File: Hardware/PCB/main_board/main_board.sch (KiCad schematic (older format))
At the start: 0 parts

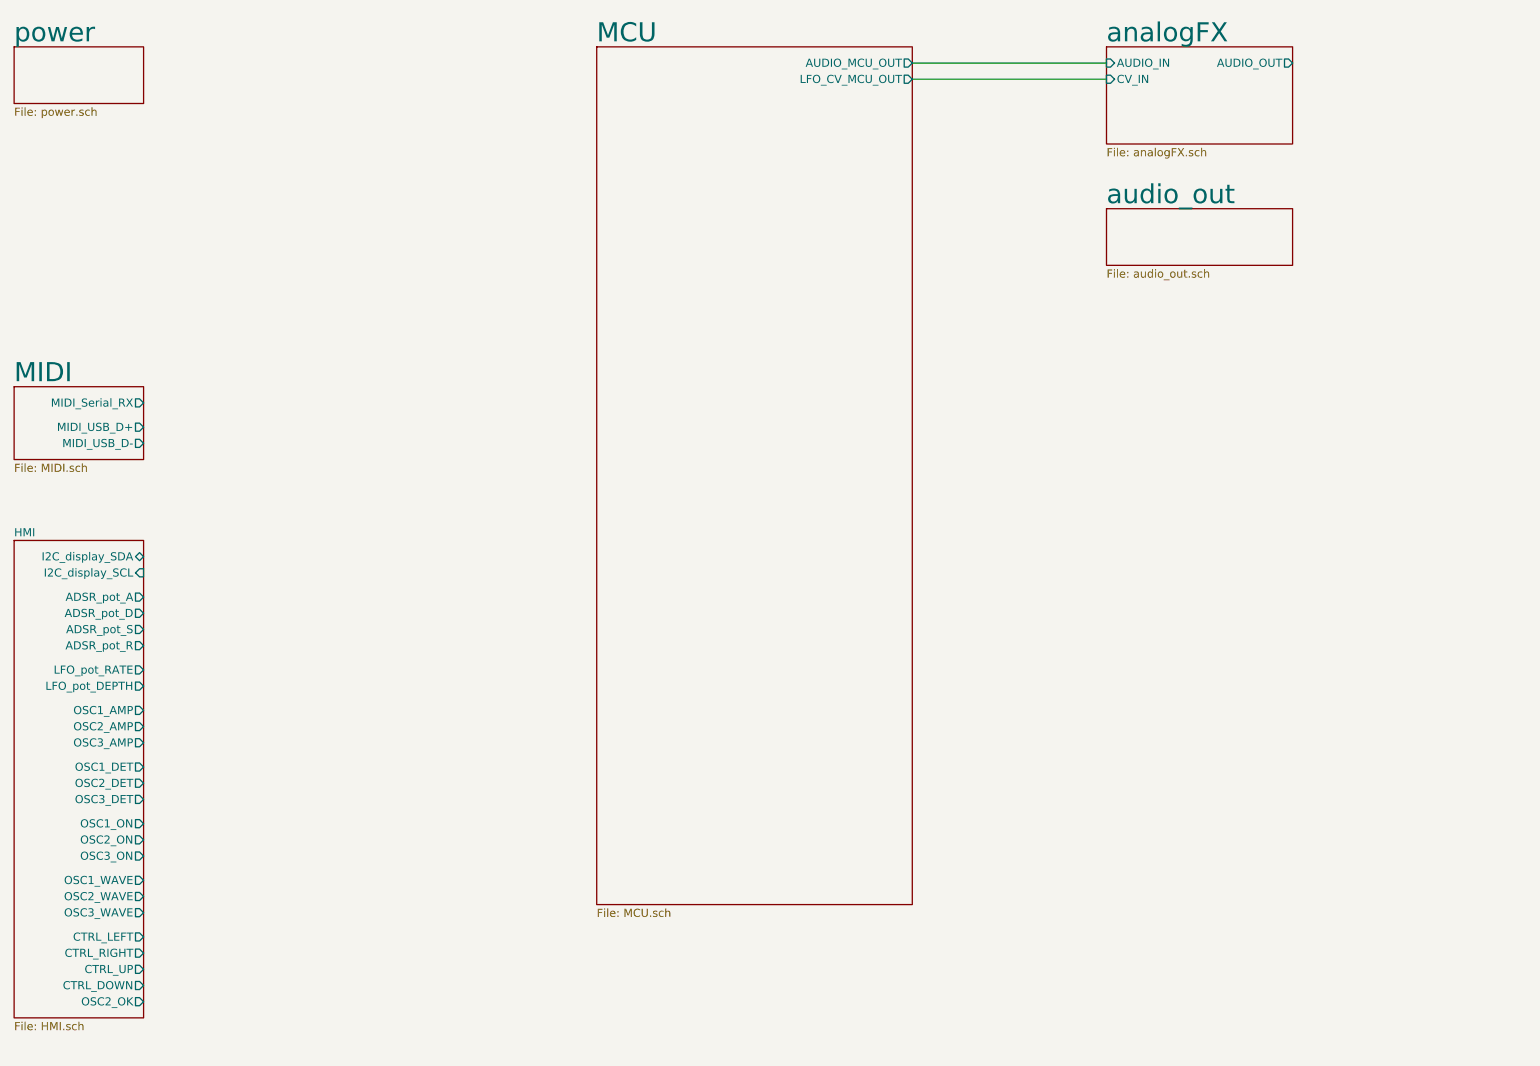
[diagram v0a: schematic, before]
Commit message: Place VCF components, I2C bus
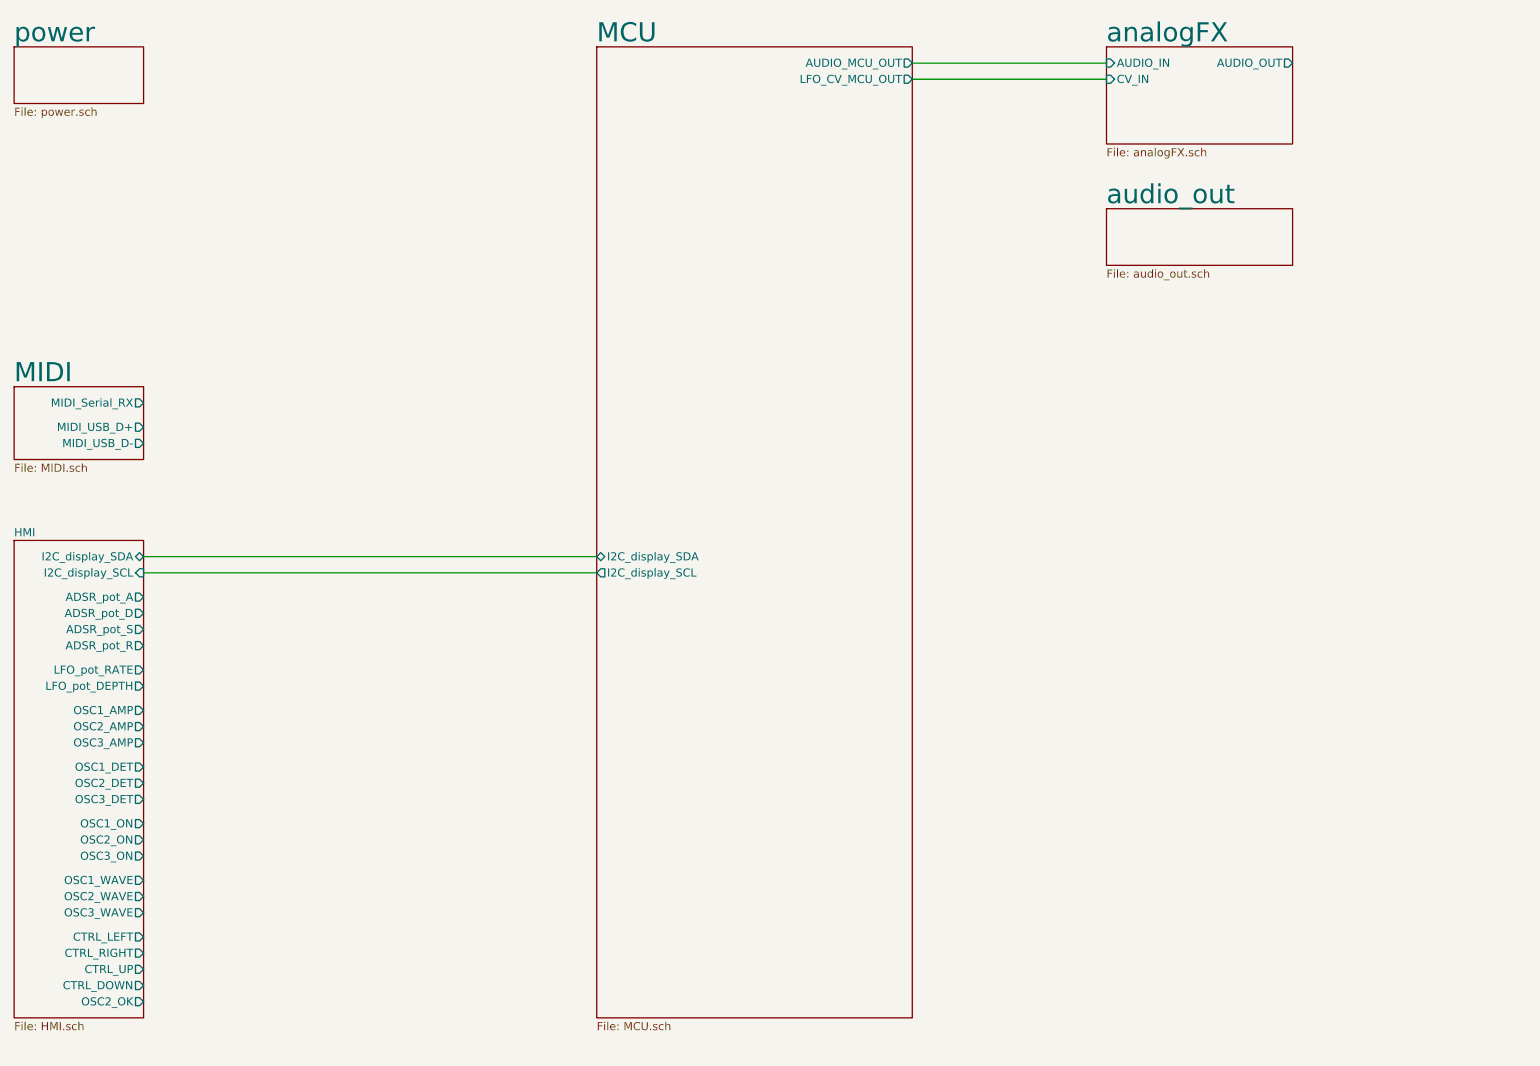
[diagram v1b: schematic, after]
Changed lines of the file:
@@
-$EndSheet
-$Sheet
-S 4800 1150 1950 5300
-U 5E658709
-F0 "MCU" 118
-F1 "MCU.sch" 50
-F2 "AUDIO_MCU_OUT" O R 6750 1250 50
-F3 "LFO_CV_MCU_OUT" O R 6750 1350 50
 $EndSheet
 $Sheet
@@
 F26 "LFO_pot_DEPTH" O R 2000 5100 50
 $EndSheet
+$Sheet
+S 4800 1150 1950 6000
+U 5E658709
+F0 "MCU" 118
+F1 "MCU.sch" 50
+F2 "AUDIO_MCU_OUT" O R 6750 1250 50
+F3 "LFO_CV_MCU_OUT" O R 6750 1350 50
+F4 "I2C_display_SCL" O L 4800 4400 50
+F5 "I2C_display_SDA" B L 4800 4300 50
+$EndSheet
+Wire Wire Line
+	2000 4300 4800 4300
+Wire Wire Line
+	4800 4400 2000 4400
 $EndSCHEMATC

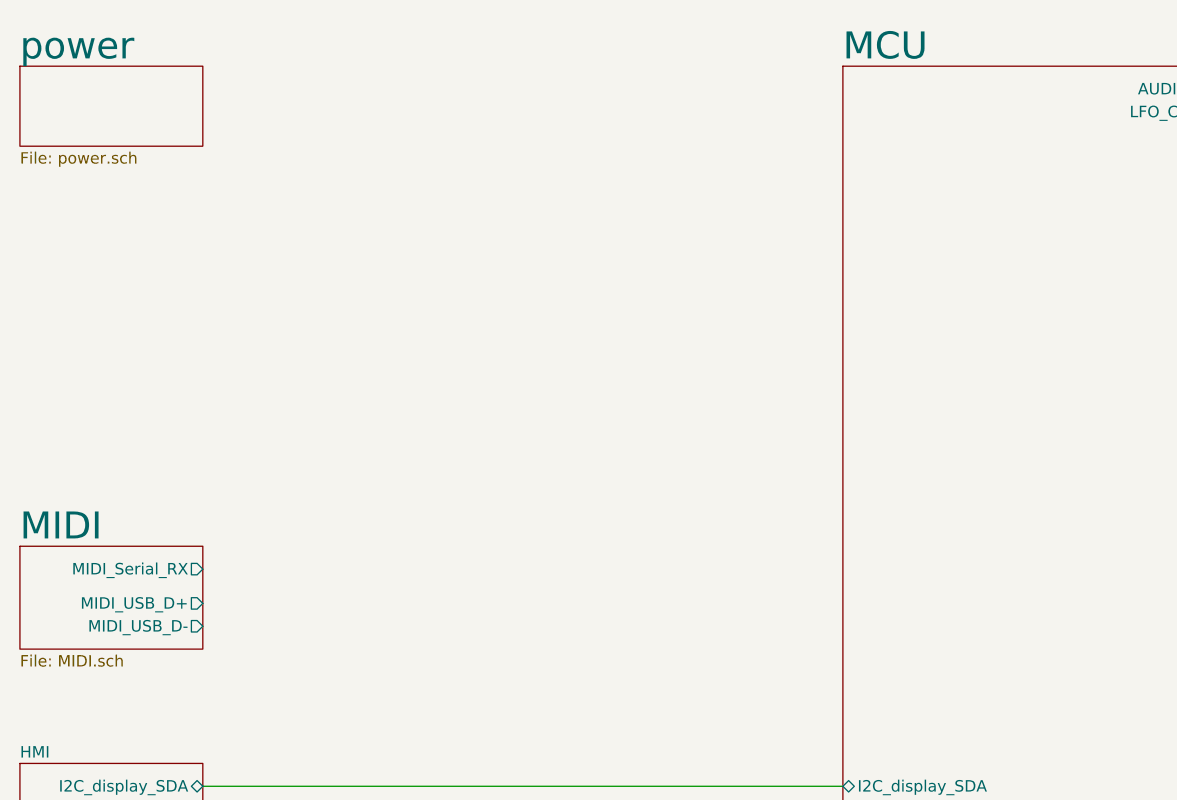
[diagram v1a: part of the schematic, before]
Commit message: Update 3D view
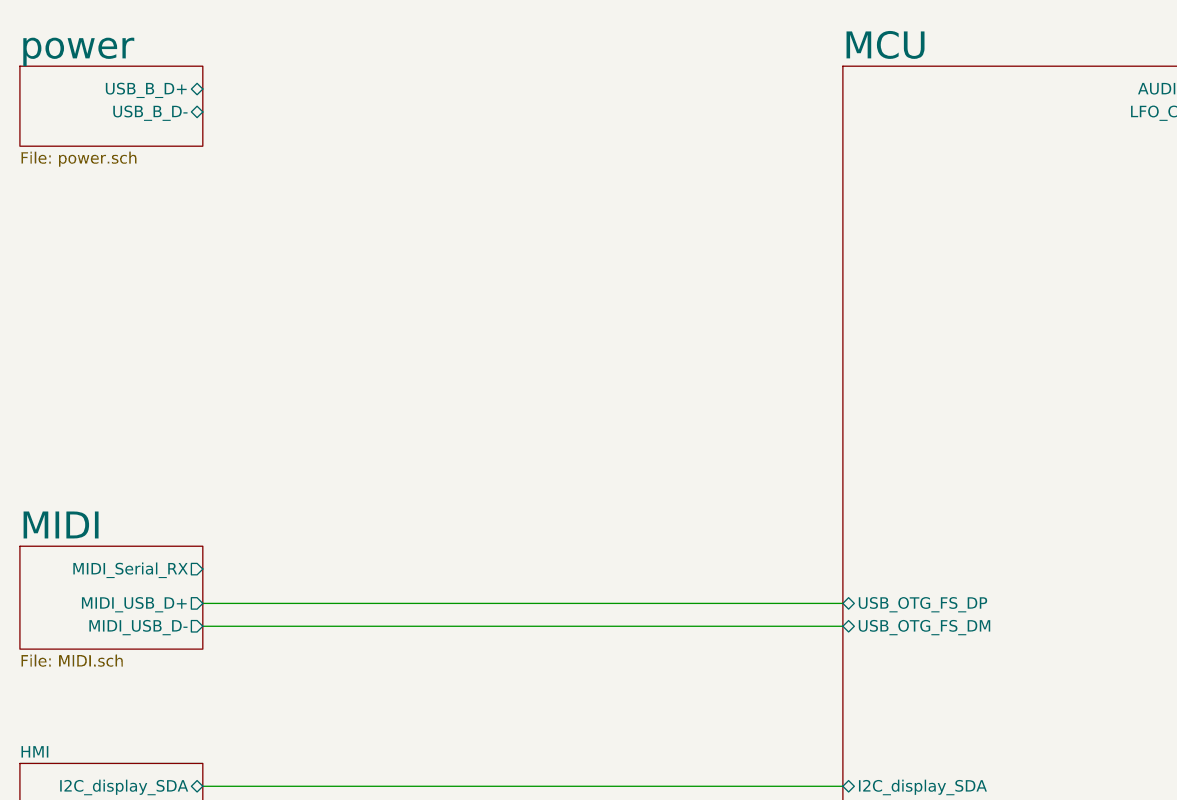
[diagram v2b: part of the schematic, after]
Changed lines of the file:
@@
 F0 "power" 118
 F1 "power.sch" 50
+F2 "USB_B_D+" B R 2000 1250 50
+F3 "USB_B_D-" B R 2000 1350 50
 $EndSheet
 $Sheet
@@
 F4 "I2C_display_SCL" O L 4800 4400 50
 F5 "I2C_display_SDA" B L 4800 4300 50
+F6 "USB_OTG_FS_DP" B L 4800 3500 50
+F7 "USB_OTG_FS_DM" B L 4800 3600 50
 $EndSheet
 Wire Wire Line
@@
 Wire Wire Line
 	4800 4400 2000 4400
+Wire Wire Line
+	2000 3500 4800 3500
+Wire Wire Line
+	2000 3600 4800 3600
 $EndSCHEMATC

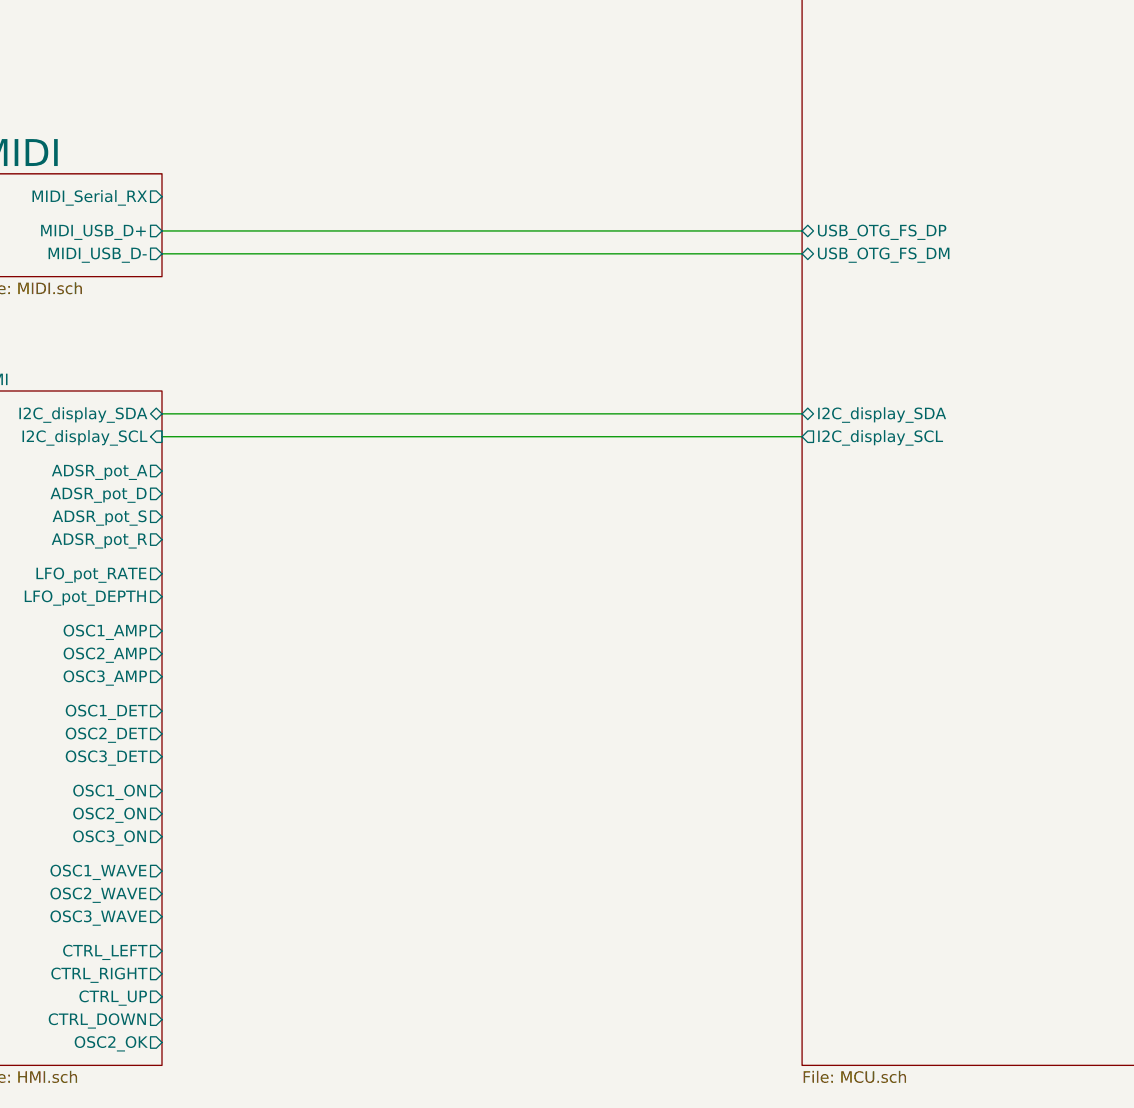
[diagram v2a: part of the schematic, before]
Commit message: Route GPIO
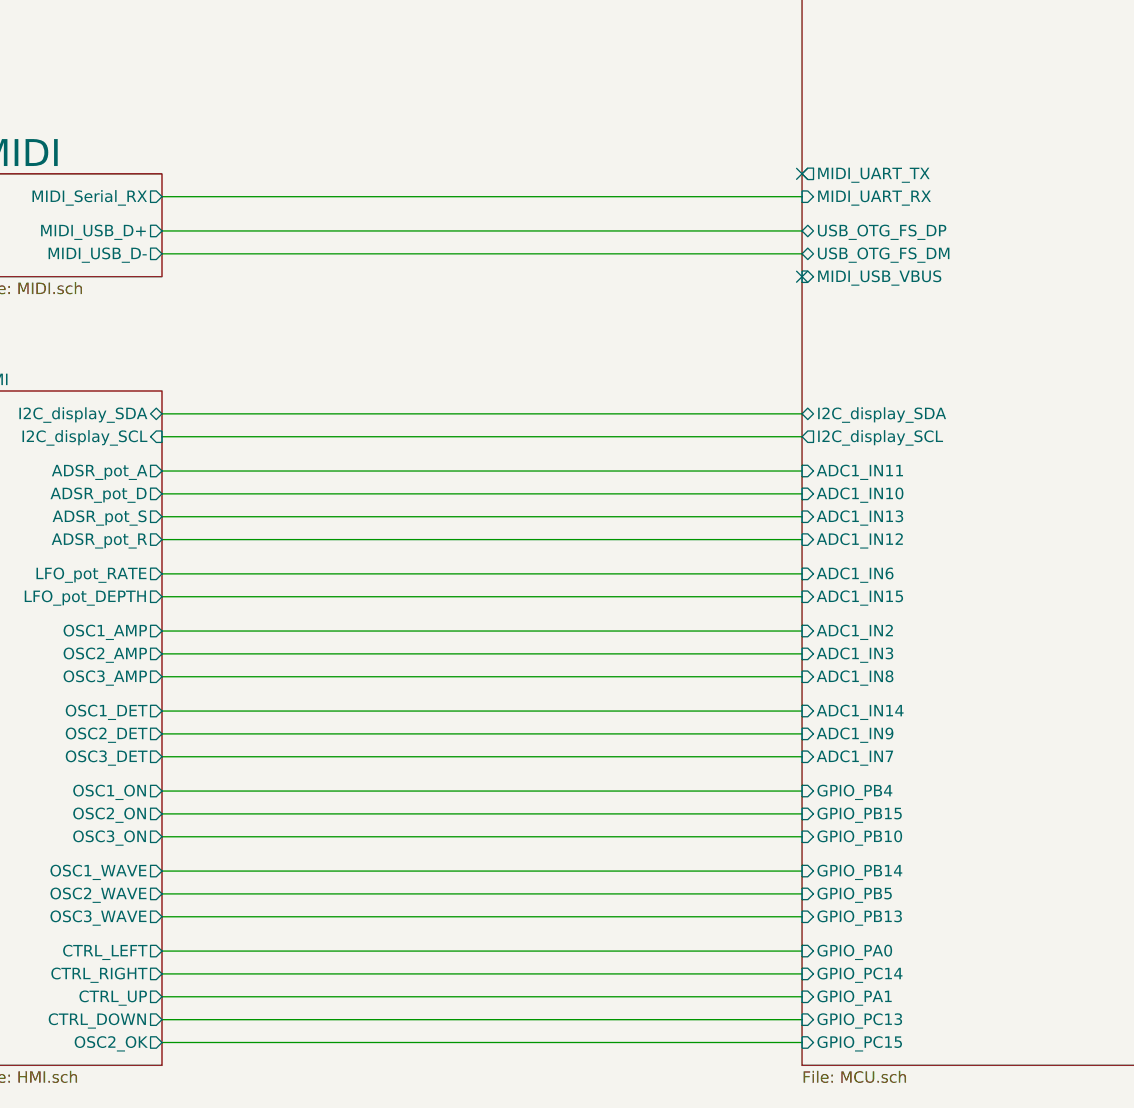
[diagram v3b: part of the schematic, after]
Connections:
- no-connect marks 0 -> 2
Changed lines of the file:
@@
 F26 "LFO_pot_DEPTH" O R 2000 5100 50
 $EndSheet
+Wire Wire Line
+	2000 4300 4800 4300
+Wire Wire Line
+	4800 4400 2000 4400
+Wire Wire Line
+	2000 3500 4800 3500
+Wire Wire Line
+	2000 3600 4800 3600
+Wire Wire Line
+	2000 5000 4800 5000
+Wire Wire Line
+	4800 5100 2000 5100
+Wire Wire Line
+	2000 4550 4800 4550
+Wire Wire Line
+	4800 4650 2000 4650
+Wire Wire Line
+	2000 4750 4800 4750
+Wire Wire Line
+	4800 4850 2000 4850
+Wire Wire Line
+	2000 5250 4800 5250
+Wire Wire Line
+	4800 5350 2000 5350
+Wire Wire Line
+	2000 5450 4800 5450
+Wire Wire Line
+	4800 5600 2000 5600
+Wire Wire Line
+	2000 5700 4800 5700
+Wire Wire Line
+	4800 5800 2000 5800
+Wire Wire Line
+	4800 6650 2000 6650
+Wire Wire Line
+	2000 6750 4800 6750
+Wire Wire Line
+	4800 6850 2000 6850
+Wire Wire Line
+	2000 6950 4800 6950
+Wire Wire Line
+	4800 7050 2000 7050
 $Sheet
 S 4800 1150 1950 6000
@@
 F6 "USB_OTG_FS_DP" B L 4800 3500 50
 F7 "USB_OTG_FS_DM" B L 4800 3600 50
+F8 "MIDI_UART_TX" O L 4800 3250 50
+F9 "MIDI_UART_RX" I L 4800 3350 50
+F10 "MIDI_USB_VBUS" I L 4800 3700 50
+F11 "ADC1_IN10" I L 4800 4650 50
+F12 "ADC1_IN11" I L 4800 4550 50
+F13 "ADC1_IN12" I L 4800 4850 50
+F14 "ADC1_IN13" I L 4800 4750 50
+F15 "ADC1_IN2" I L 4800 5250 50
+F16 "ADC1_IN3" I L 4800 5350 50
+F17 "ADC1_IN6" I L 4800 5000 50
+F18 "ADC1_IN7" I L 4800 5800 50
+F19 "ADC1_IN14" I L 4800 5600 50
+F20 "ADC1_IN15" I L 4800 5100 50
+F21 "ADC1_IN9" I L 4800 5700 50
+F22 "ADC1_IN8" I L 4800 5450 50
+F23 "GPIO_PA0" I L 4800 6650 50
+F24 "GPIO_PA1" I L 4800 6850 50
+F25 "GPIO_PC13" I L 4800 6950 50
+F26 "GPIO_PC14" I L 4800 6750 50
+F27 "GPIO_PC15" I L 4800 7050 50
+F28 "GPIO_PB13" I L 4800 6500 50
+F29 "GPIO_PB14" I L 4800 6300 50
+F30 "GPIO_PB15" I L 4800 6050 50
+F31 "GPIO_PB4" I L 4800 5950 50
+F32 "GPIO_PB5" I L 4800 6400 50
+F33 "GPIO_PB10" I L 4800 6150 50
 $EndSheet
 Wire Wire Line
-	2000 4300 4800 4300
+	4800 5950 2000 5950
 Wire Wire Line
-	4800 4400 2000 4400
+	2000 6050 4800 6050
 Wire Wire Line
-	2000 3500 4800 3500
+	4800 6150 2000 6150
 Wire Wire Line
-	2000 3600 4800 3600
+	2000 6300 4800 6300
+Wire Wire Line
+	4800 6400 2000 6400
+Wire Wire Line
+	2000 6500 4800 6500
+Wire Wire Line
+	2000 3350 4800 3350
+NoConn ~ 4800 3250
+NoConn ~ 4800 3700
 $EndSCHEMATC

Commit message: Route PWR
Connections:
- no-connect marks 2 -> 4
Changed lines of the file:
@@
 NoConn ~ 4800 3250
 NoConn ~ 4800 3700
+NoConn ~ 2000 1250
+NoConn ~ 2000 1350
 $EndSCHEMATC

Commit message: Change GPIO config
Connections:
- no-connect marks 4 -> 2
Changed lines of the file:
@@
 encoding utf-8
 Sheet 1 7
-Title ""
-Date ""
-Rev ""
-Comp ""
-Comment1 ""
+Title "MiniMood"
+Date "2020"
+Rev "A"
+Comp "INSA Rennes"
+Comment1 "Heol Fief, Vincent Colombel, Julien le Pelve, Loïc Scotto"
 Comment2 ""
 Comment3 ""
@@
 F27 "GPIO_PC15" I L 4800 7050 50
 F28 "GPIO_PB13" I L 4800 6500 50
-F29 "GPIO_PB14" I L 4800 6300 50
-F30 "GPIO_PB15" I L 4800 6050 50
-F31 "GPIO_PB4" I L 4800 5950 50
-F32 "GPIO_PB5" I L 4800 6400 50
-F33 "GPIO_PB10" I L 4800 6150 50
+F29 "GPIO_PB4" I L 4800 5950 50
+F30 "GPIO_PB5" I L 4800 6400 50
+F31 "GPIO_PB10" I L 4800 6150 50
+F32 "GPIO_PB8" I L 4800 6300 50
+F33 "GPIO_PB9" I L 4800 6050 50
+F34 "USB_DEV_HS_DM" B L 4800 1350 50
+F35 "USB_DEV_HS_DP" B L 4800 1250 50
 $EndSheet
 Wire Wire Line
@@
 NoConn ~ 4800 3250
 NoConn ~ 4800 3700
-NoConn ~ 2000 1250
-NoConn ~ 2000 1350
+Wire Wire Line
+	2000 1250 4800 1250
+Wire Wire Line
+	4800 1350 2000 1350
 $EndSCHEMATC

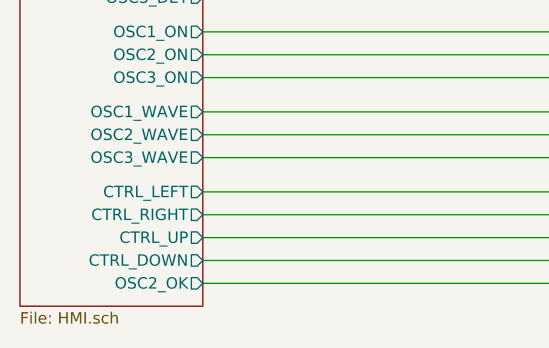
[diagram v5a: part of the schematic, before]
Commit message: Label GPIO, create HMI files
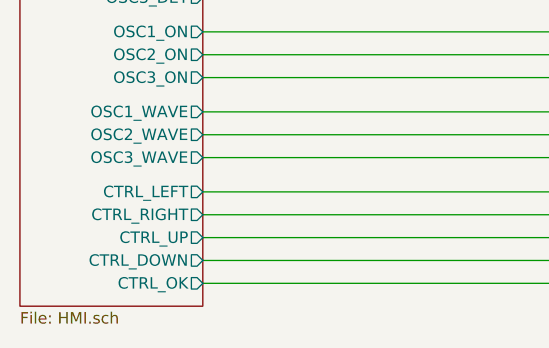
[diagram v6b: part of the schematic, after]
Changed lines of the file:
@@
 F22 "CTRL_UP" O R 2000 6850 50
 F23 "CTRL_DOWN" O R 2000 6950 50
-F24 "OSC2_OK" O R 2000 7050 50
-F25 "LFO_pot_RATE" O R 2000 5000 50
-F26 "LFO_pot_DEPTH" O R 2000 5100 50
+F24 "LFO_pot_RATE" O R 2000 5000 50
+F25 "LFO_pot_DEPTH" O R 2000 5100 50
+F26 "CTRL_OK" O R 2000 7050 50
 $EndSheet
 Wire Wire Line
